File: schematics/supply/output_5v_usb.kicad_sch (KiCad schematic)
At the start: 82 parts, among them J2 USB_A, Q3 40N06, U10 IRS2153S, U11 LM2904, U12 IP2163, U13 LM2904, U14 TL432DBZ, U15 LM2904, U16 AMS1117-3.3, U2 EL817, U6 INA3221, U8 MC34063AD, U9 TL432DBZ

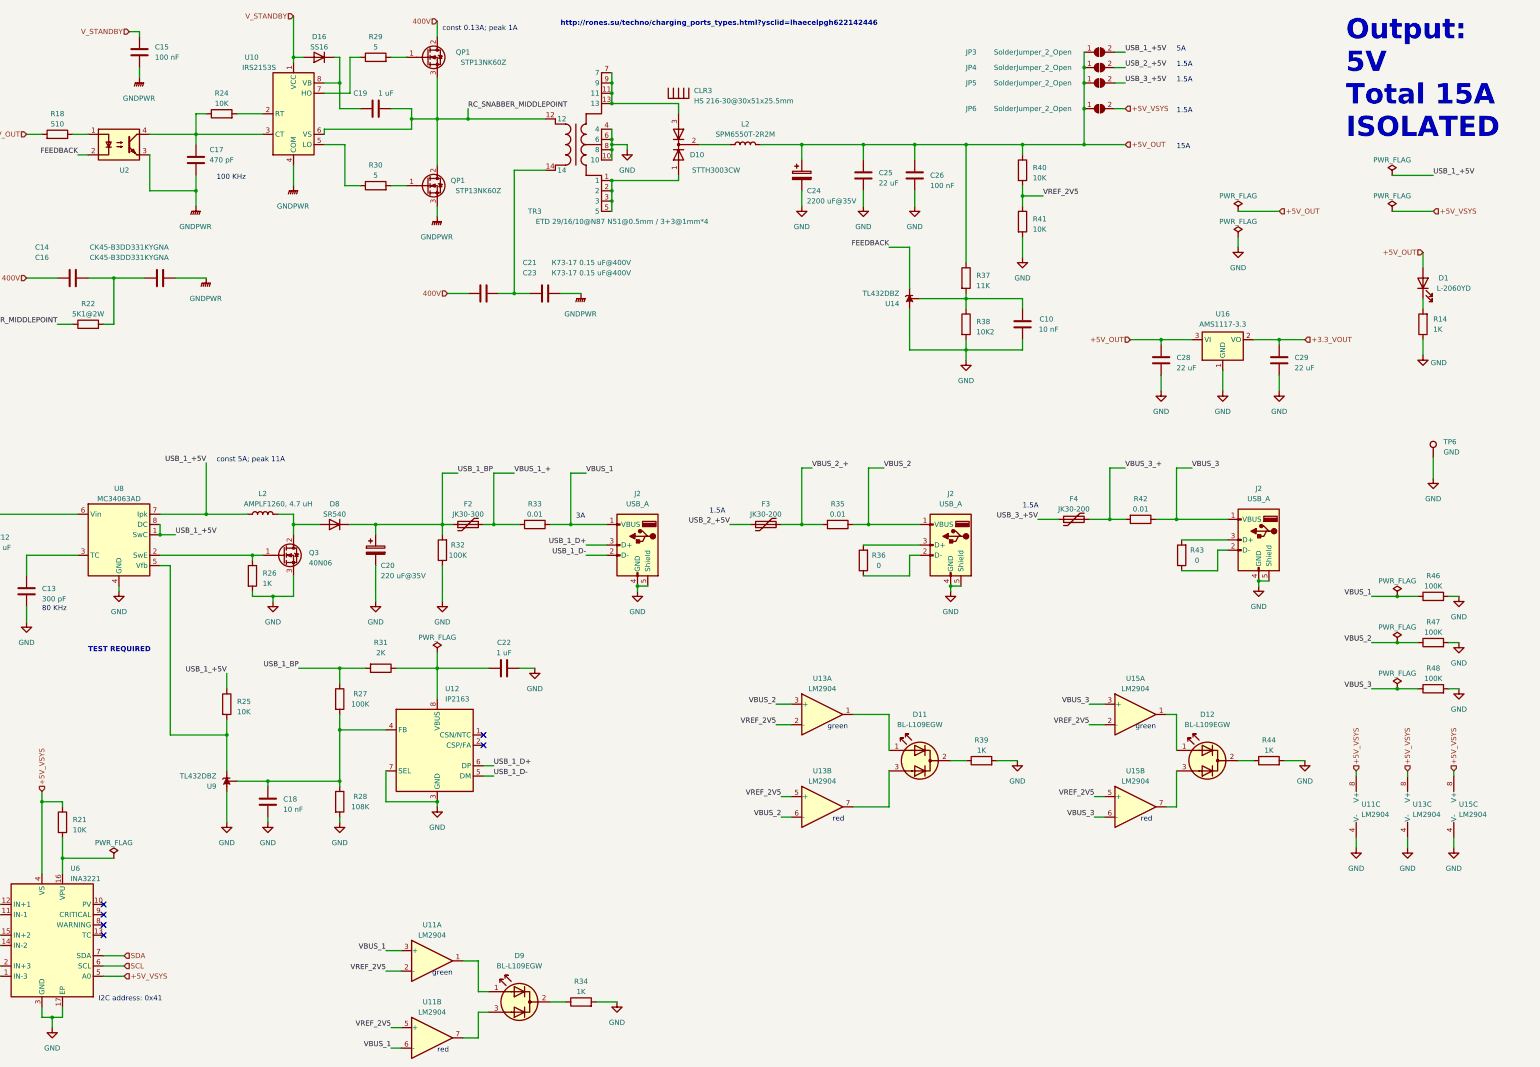
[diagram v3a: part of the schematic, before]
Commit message: little changes in schematics
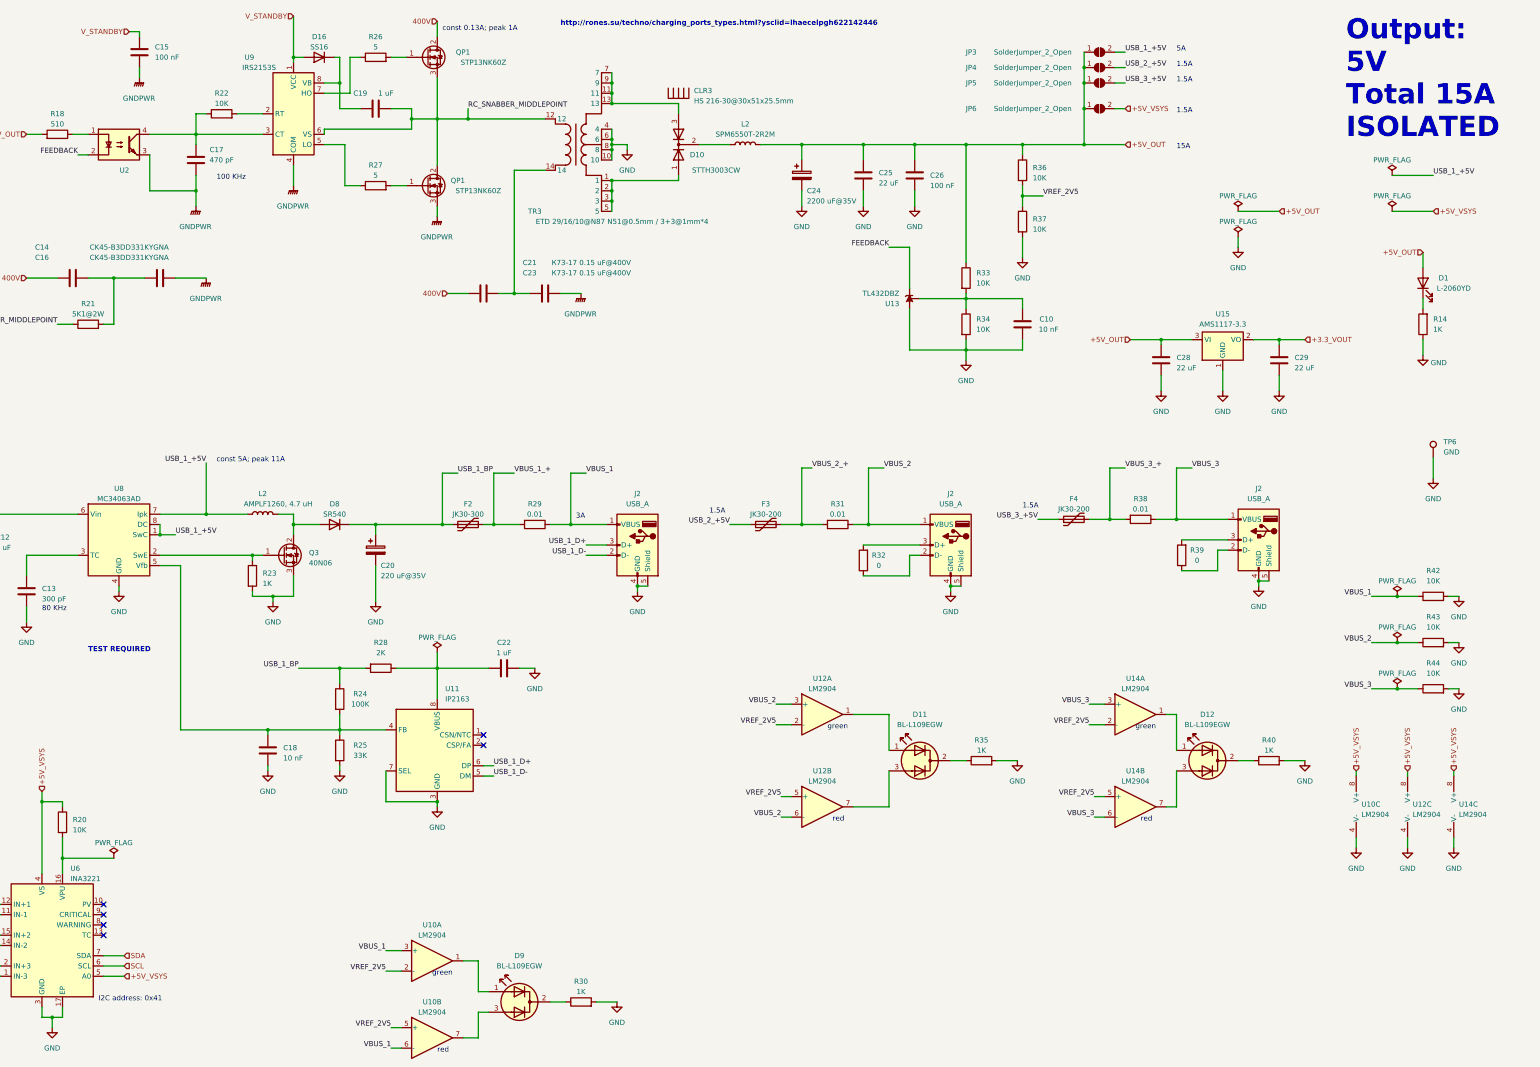
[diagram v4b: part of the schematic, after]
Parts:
- removed R25: 10K, Resistor_SMD:R_0805_2012Metric, symbol Device:R
- removed R32: 100K, Resistor_SMD:R_0805_2012Metric, symbol Device:R
- removed U9: TL432DBZ, Package_TO_SOT_SMD:SOT-23-3, symbol Reference_Voltage:TL432DBZ
- R25: renamed from R28; value 108K -> 33K
- R33: renamed from R37; value 11K -> 10K
- R34: renamed from R38; value 10K2 -> 10K
- R42: renamed from R46; value 100K -> 10K
- R43: renamed from R47; value 100K -> 10K
- R44: renamed from R48; value 100K -> 10K
- renumbered R21 to R20, R22 to R21, R24 to R22, R26 to R23, R27 to R24, R29 to R26, R30 to R27, R31 to R28, R33 to R29, R34 to R30, R35 to R31, R36 to R32, R39 to R35, R40 to R36, R41 to R37, R42 to R38, R43 to R39, R44 to R40, U11 to U10, U12 to U11, U13 to U12, U14 to U13, U15 to U14, U16 to U15, U10 to U9
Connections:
- net at U8.5 (Vfb): now also C18.2, R24.2, R25.1, U11.4 (FB)
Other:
- moved on the sheet: C18, R25
